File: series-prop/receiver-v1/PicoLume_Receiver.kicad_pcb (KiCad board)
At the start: 2 copper layers, 47 x 84.9 mm, 69 parts, among them IC1 LM66200DRLR, J1 Conn_01x17, J10 Conn_01x03_Pin, J11 Conn_01x04_Pin, J13 USB_C_Receptacle_USB2.0_16P, J2 Conn_01x04_Pin, J4 Conn_01x17, J5 Conn_01x01_Pin, J6 Screw_Terminal_01x02, J7 Screw_Terminal_01x03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

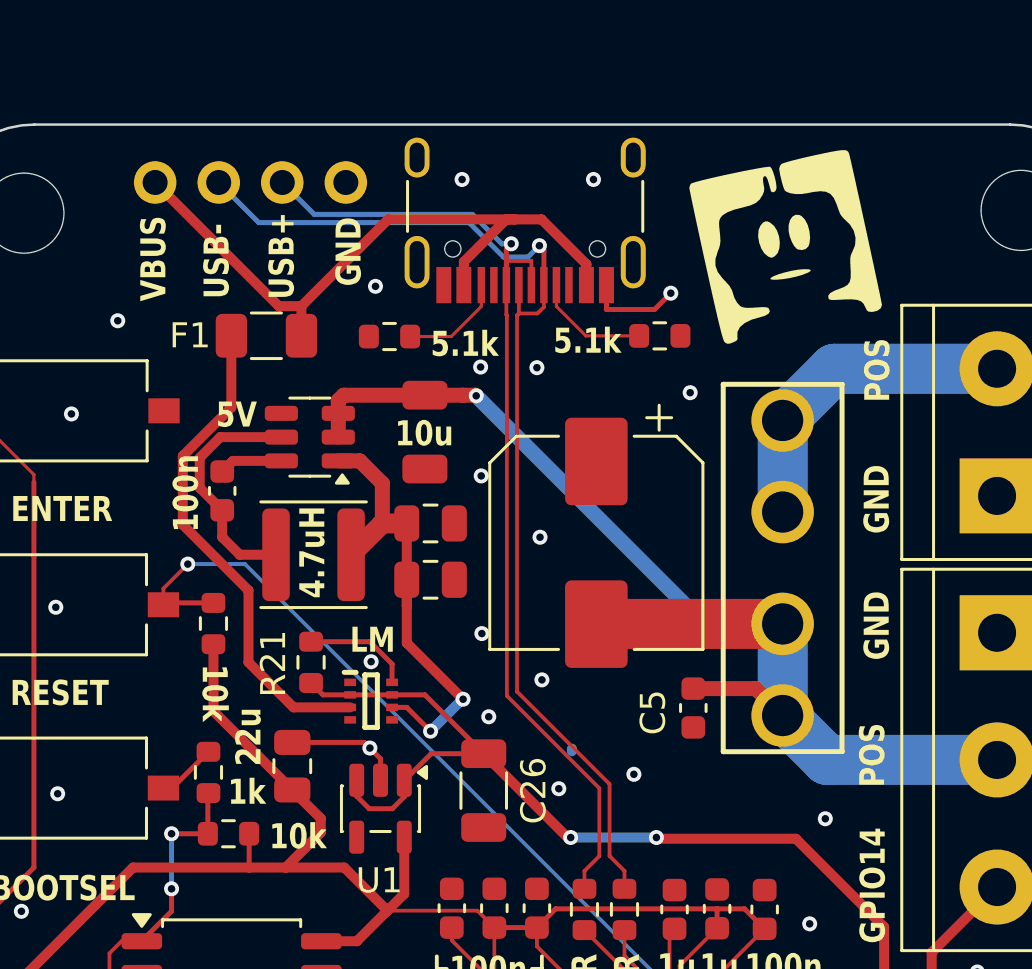
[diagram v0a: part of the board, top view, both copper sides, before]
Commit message: Removed bulk output cap and added PTC on VBAT input
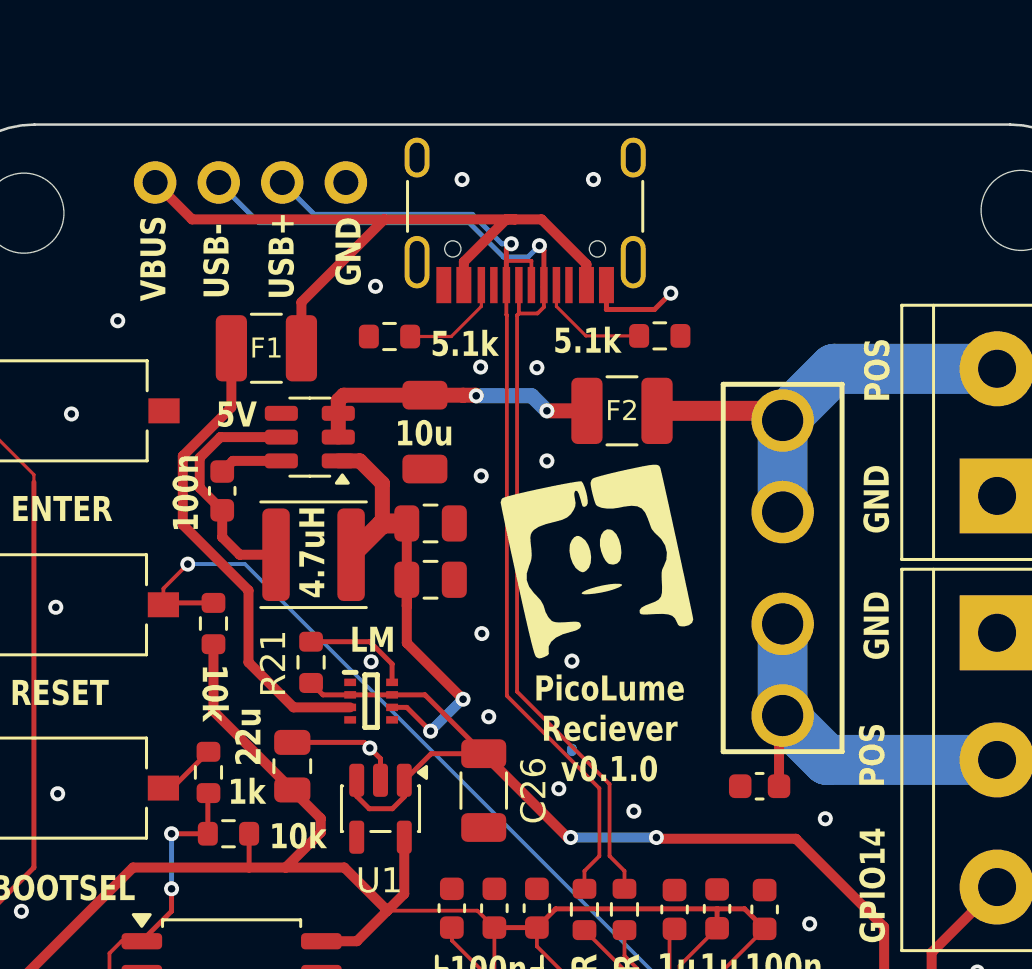
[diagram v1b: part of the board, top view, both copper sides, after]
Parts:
- removed C4: 220uF, Capacitor_SMD:CP_Elec_8x10
- added F2: Polyfuse, Fuse:Fuse_1210_3225Metric, F.Cu at (127.5, 74.5)
- F1: footprint Fuse:Fuse_1206_3216Metric -> Fuse:Fuse_1210_3225Metric
- moved G*** 14.7 mm to (126.5, 80.5)
- moved C5 4.10 mm to (133.0, 89.5), turned to 0 degrees
- moved F1 0.50 mm to (113.3, 72.0)
- renumbered 100n to C21
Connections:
- C18 pad 1: FUSED -> Net-(U5-EN)
- U5 pad 2: FUSED -> Net-(U5-EN)
- U5 pad 3: FUSED -> Net-(U5-EN)
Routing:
- net FUSED: track 47.5 -> 16.1 mm, vias 1 -> 0
- net Net-(U5-EN): track 0.00 -> 11.7 mm, vias 0 -> 2
- net VBAT: track 13.1 -> 18.3 mm
- net VBUS: track 27.2 -> 29.6 mm
- net GND: vias 68 -> 67
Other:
- board text added: "PicoLume Reciever v0.1.0"

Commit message: replaced the RGB led with a button on GPIO15
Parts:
- removed C21, C5: 100n, Capacitor_SMD:C_0603_1608Metric
- removed D2: WS2812B-2020, LED_SMD:LED_WS2812B-2020_PLCC4_2.0x2.0mm
- added SW4: SW_Push, Button_Switch_SMD:SW_Tactile_SPST_NO_Straight_CK_PTS636Sx25SMTRLFS, F.Cu at (128.8, 120.3)
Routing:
- net +5V: track 75.8 -> 45.3 mm, vias 3 -> 2
- net /GPIO15: track 53.6 -> 57.2 mm
- net FUSED: track 16.1 -> 13.4 mm
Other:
- board text added: "6V-30V"
- board text added: "CONFIG"
- board text added: "I2C"
- board text added: "POS 6V-30V"
- board text added: "Warning: GPIO 14 is level-shifted to 5V at the terminal block Warning: Use internal pullup resistor for the ENTER button connected to GPIO3 and GPIO15"
- board text removed: "GPIO15"
- board text removed: "Input Voltage 6v - 30V"
- board text removed: "Qwiic"
- board text removed: "RGB"
- board text removed: "Warning: GPIO 14 is level-shifted to 5V at the terminal block Warning: Use internal pullup resistor for the ENTER button connected to GPIO3"
